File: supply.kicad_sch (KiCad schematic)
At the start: 35 parts

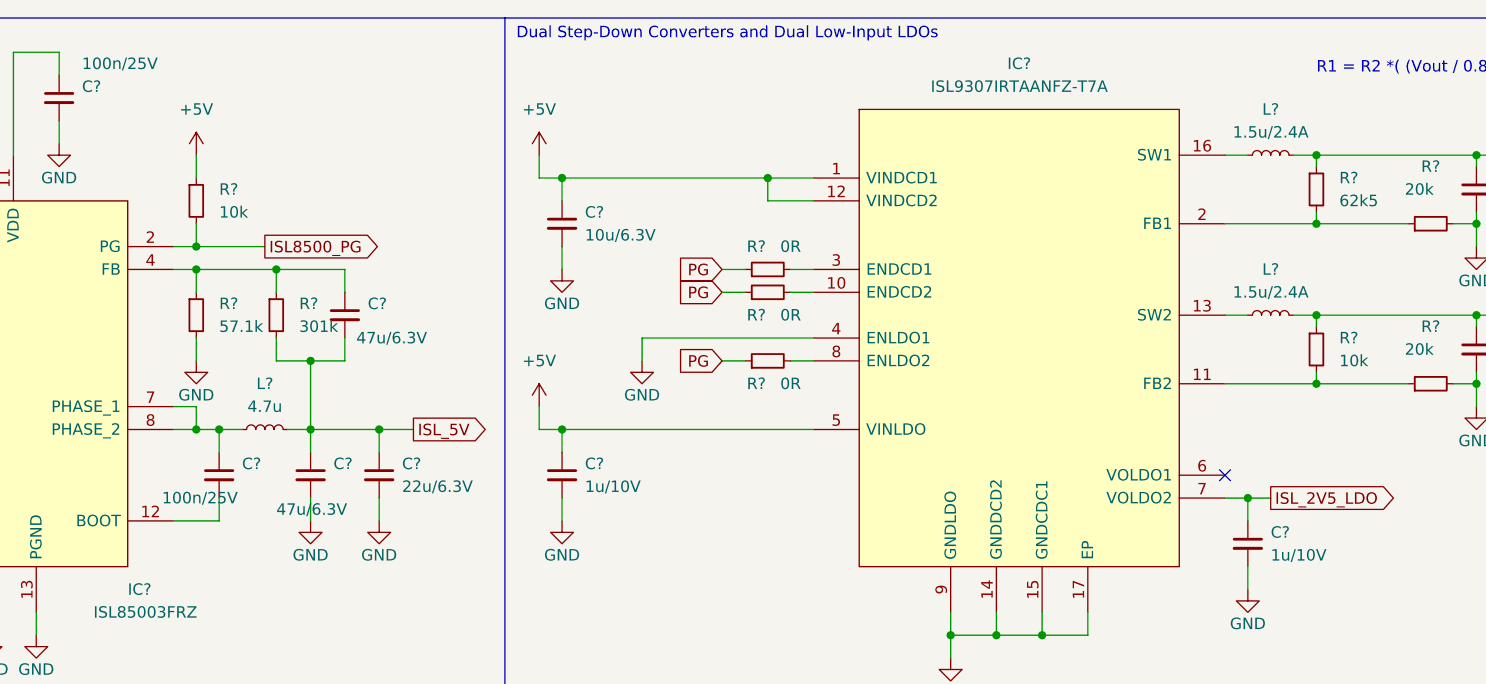
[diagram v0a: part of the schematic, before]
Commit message: added missing MNR && footprint to inductor added footprint to test points
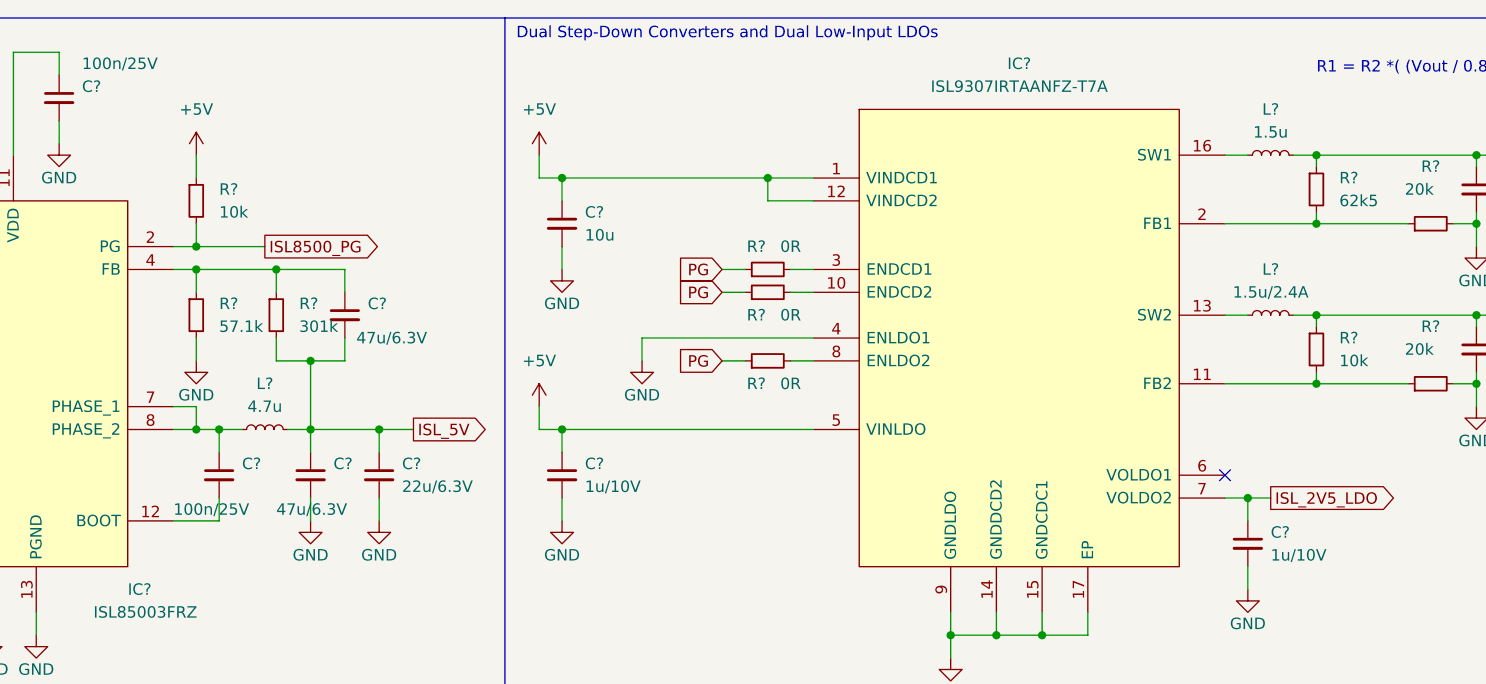
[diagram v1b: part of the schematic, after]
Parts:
- removed C?: 1u/10V, Capacitor_SMD:C_0603_1608Metric_Pad1.08x0.95mm_HandSolder, symbol Device:C_Small
- removed C?: 100n/25V, Capacitor_SMD:C_0603_1608Metric_Pad1.08x0.95mm_HandSolder, symbol Device:C_Small
- added C?: 100n/25V, Capacitor_SMD:C_0603_1608Metric_Pad1.08x0.95mm_HandSolder, symbol Device:C_Small
- added C?: 1u/10V, Capacitor_SMD:C_0603_1608Metric_Pad1.08x0.95mm_HandSolder, symbol Device:C_Small
- C?: value 10u/6.3V -> 10u
- L?: value 1.5u/2.4A -> 1.5u
- L?: footprint (none) -> supply:NR5040T4R7N; MNR (none) -> 963-NR5040T4R7N
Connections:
- net +5V: now also C?.1
- net GND: now also C?.2
- net at IC?.12 (BOOT): now also C?.2
- net at IC?.7 (PHASE_1), IC?.8 (PHASE_2), L?.1: now also C?.1
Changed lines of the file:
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@@
       (effects (font (size 1.27 1.27)) (justify left))
     )
-    (property "Value" "10u/6.3V" (id 1) (at 135.89 49.5362 0)
+    (property "Value" "10u" (id 1) (at 135.89 49.5362 0)
       (effects (font (size 1.27 1.27)) (justify left))
     )
@@
     (in_bom yes) (on_board yes) (fields_autoplaced)
     (property "Reference" "L?" (id 0) (at 212.09 35.56 90))
-    (property "Value" "1.5u/2.4A" (id 1) (at 212.09 38.1 90))
+    (property "Value" "1.5u" (id 1) (at 212.09 38.1 90))
     (property "Footprint" "Inductor_SMD:L_1008_2520Metric_Pad1.43x2.20mm_HandSolder" (id 2) (at 212.09 40.64 0)
       (effects (font (size 1.27 1.27)) hide)
@@
     )
     (property "MNR" " 963-MAKK2520H1R5M " (id 5) (at 212.09 40.64 90)
-      (effects (font (size 1.27 1.27)) hide)
-    )
-    (pin "1")
-    (pin "2")
-  )
-  (symbol (lib_id "Device:C_Small") (at 133.35 76.2 0) (unit 1)
-    (in_bom yes) (on_board yes) (fields_autoplaced)
-    (property "Reference" "C?" (id 0) (at 135.89 74.9362 0)
-      (effects (font (size 1.27 1.27)) (justify left))
-    )
-    (property "Value" "1u/10V" (id 1) (at 135.89 77.4762 0)
-      (effects (font (size 1.27 1.27)) (justify left))
-    )
-    (property "Footprint" "Capacitor_SMD:C_0603_1608Metric_Pad1.08x0.95mm_HandSolder" (id 2) (at 133.35 76.2 0)
-      (effects (font (size 1.27 1.27)) hide)
-    )
-    (property "Datasheet" "~" (id 3) (at 133.35 76.2 0)
-      (effects (font (size 1.27 1.27)) hide)
-    )
-    (property "MNR" " 187-CL10A105KP8NNWC " (id 5) (at 133.35 76.2 0)
       (effects (font (size 1.27 1.27)) hide)
     )
@@
     (pin "2")
   )
+  (symbol (lib_id "Device:C_Small") (at 95.25 76.2 0) (unit 1)
+    (in_bom yes) (on_board yes)
+    (property "Reference" "C?" (id 0) (at 97.79 74.9362 0)
+      (effects (font (size 1.27 1.27)) (justify left))
+    )
+    (property "Value" "100n/25V" (id 1) (at 90.17 80.01 0)
+      (effects (font (size 1.27 1.27)) (justify left))
+    )
+    (property "Footprint" "Capacitor_SMD:C_0603_1608Metric_Pad1.08x0.95mm_HandSolder" (id 2) (at 95.25 76.2 0)
+      (effects (font (size 1.27 1.27)) hide)
+    )
+    (property "Datasheet" "~" (id 3) (at 95.25 76.2 0)
+      (effects (font (size 1.27 1.27)) hide)
+    )
+    (property "MNR" " 603-CC603KRX7R8BB104 " (id 5) (at 95.25 76.2 0)
+      (effects (font (size 1.27 1.27)) hide)
+    )
+    (pin "1")
+    (pin "2")
+  )
   (symbol (lib_id "power:+5V") (at 114.3 114.3 0) (unit 1)
     (in_bom yes) (on_board yes) (fields_autoplaced)
@@
     (property "Reference" "L?" (id 0) (at 100.33 66.04 90))
     (property "Value" "4.7u" (id 1) (at 100.33 68.58 90))
-    (property "Footprint" "" (id 2) (at 100.33 71.12 0)
+    (property "Footprint" "supply:NR5040T4R7N" (id 2) (at 100.33 71.12 0)
       (effects (font (size 1.27 1.27)) hide)
     )
     (property "Datasheet" "~" (id 3) (at 100.33 71.12 0)
+      (effects (font (size 1.27 1.27)) hide)
+    )
+    (property "MNR" " 963-NR5040T4R7N " (id 5) (at 100.33 71.12 90)
       (effects (font (size 1.27 1.27)) hide)
     )
@@
     (pin "1")
   )
-  (symbol (lib_id "Device:C_Small") (at 95.25 76.2 0) (unit 1)
-    (in_bom yes) (on_board yes)
-    (property "Reference" "C?" (id 0) (at 97.79 74.9362 0)
-      (effects (font (size 1.27 1.27)) (justify left))
-    )
-    (property "Value" "100n/25V" (id 1) (at 88.9 78.74 0)
-      (effects (font (size 1.27 1.27)) (justify left))
-    )
-    (property "Footprint" "Capacitor_SMD:C_0603_1608Metric_Pad1.08x0.95mm_HandSolder" (id 2) (at 95.25 76.2 0)
-      (effects (font (size 1.27 1.27)) hide)
-    )
-    (property "Datasheet" "~" (id 3) (at 95.25 76.2 0)
-      (effects (font (size 1.27 1.27)) hide)
-    )
-    (property "MNR" " 603-CC603KRX7R8BB104 " (id 5) (at 95.25 76.2 0)
-      (effects (font (size 1.27 1.27)) hide)
-    )
-    (pin "1")
-    (pin "2")
-  )
   (symbol (lib_id "Device:R_Small") (at 229.87 66.04 90) (unit 1)
     (in_bom yes) (on_board yes)
@@
     (pin "1")
   )
+  (symbol (lib_id "Device:C_Small") (at 133.35 76.2 0) (unit 1)
+    (in_bom yes) (on_board yes) (fields_autoplaced)
+    (property "Reference" "C?" (id 0) (at 135.89 74.9362 0)
+      (effects (font (size 1.27 1.27)) (justify left))
+    )
+    (property "Value" "1u/10V" (id 1) (at 135.89 77.4762 0)
+      (effects (font (size 1.27 1.27)) (justify left))
+    )
+    (property "Footprint" "Capacitor_SMD:C_0603_1608Metric_Pad1.08x0.95mm_HandSolder" (id 2) (at 133.35 76.2 0)
+      (effects (font (size 1.27 1.27)) hide)
+    )
+    (property "Datasheet" "~" (id 3) (at 133.35 76.2 0)
+      (effects (font (size 1.27 1.27)) hide)
+    )
+    (property "MNR" " 187-CL10A105KP8NNWC " (id 5) (at 133.35 76.2 0)
+      (effects (font (size 1.27 1.27)) hide)
+    )
+    (pin "1")
+    (pin "2")
+  )
   (symbol (lib_id "Device:R_Small") (at 156.21 55.88 90) (unit 1)

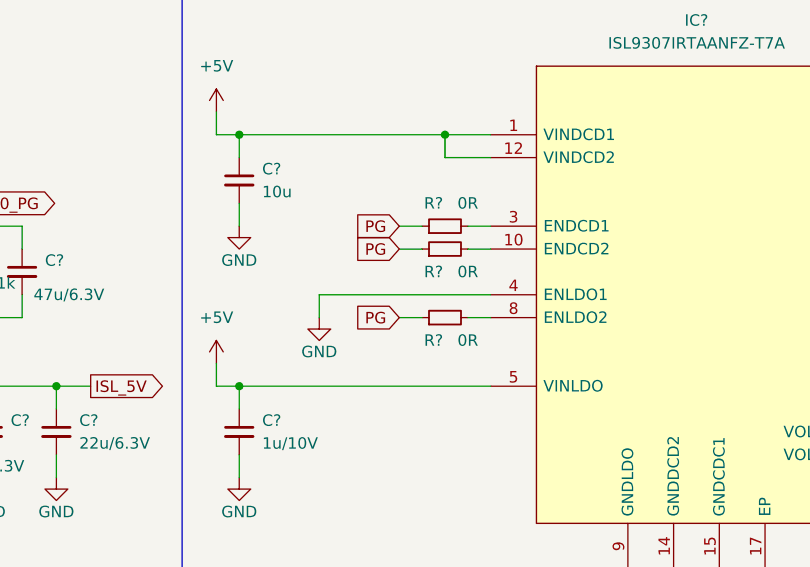
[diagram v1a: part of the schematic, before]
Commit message: fixed layout in fpga.kicad_sch
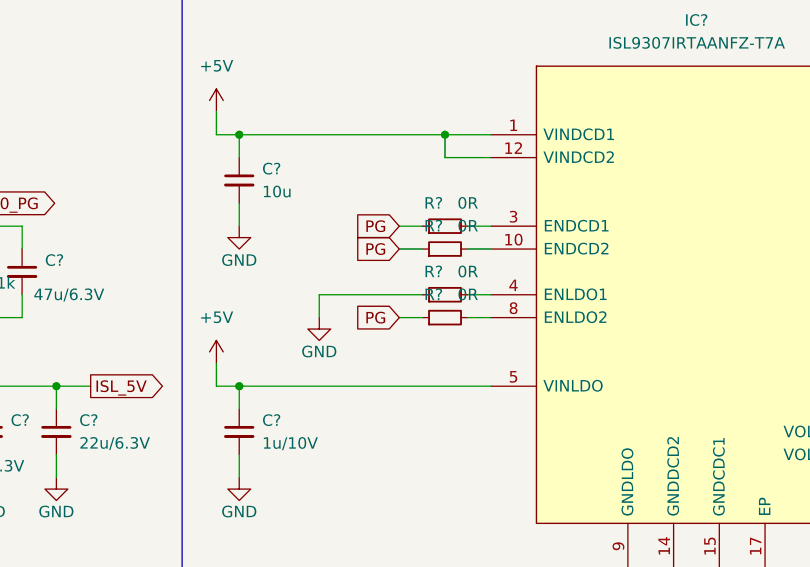
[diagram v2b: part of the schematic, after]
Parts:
- removed R?: 0R, Resistor_SMD:R_0603_1608Metric_Pad0.98x0.95mm_HandSolder, symbol Device:R_Small
- removed R?: 0R, aResistor_SMD:R_0603_1608Metric_Pad0.98x0.95mm_HandSolder, symbol Device:R_Small
- added R? (x3): 0R, Resistor_SMD:R_0603_1608Metric_Pad0.98x0.95mm_HandSolder, symbol Device:R_Small
- R?: MNR (none) -> 652-CR0603-J/-000ELF
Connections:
- net GND: now also R?.1; no longer IC?.4 (ENLDO1)
- net PG: now also R?.1, R?.1
- net at IC?.10 (ENDCD2): now also R?.2
- net at IC?.8 (ENLDO2): now also R?.2
- new net: IC?.4 (ENLDO1), R?.2
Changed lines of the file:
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@@
+    (stroke (width 0) (type default) (color 0 0 0 0))
+  )
+  (wire (pts (xy 158.75 60.96) (xy 161.29 60.96))
     (stroke (width 0) (type default) (color 0 0 0 0))
   )
@@
     (stroke (width 0) (type default) (color 0 0 0 0))
   )
+  (wire (pts (xy 142.24 60.96) (xy 153.67 60.96))
+    (stroke (width 0) (type default) (color 0 0 0 0))
+  )
   (polyline (pts (xy 139.7 101.6) (xy 140.97 101.6))
     (stroke (width 0) (type default) (color 0 0 0 0))
@@
   )
   (wire (pts (xy 50.8 138.43) (xy 53.34 138.43))
-    (stroke (width 0) (type default) (color 0 0 0 0))
-  )
-  (wire (pts (xy 142.24 60.96) (xy 161.29 60.96))
     (stroke (width 0) (type default) (color 0 0 0 0))
   )
@@
     )
     (pin "1")
+  )
+  (symbol (lib_id "Device:R_Small") (at 156.21 63.5 90) (unit 1)
+    (in_bom yes) (on_board yes)
+    (property "Reference" "R?" (id 0) (at 154.94 60.96 90))
+    (property "Value" "0R" (id 1) (at 158.75 60.96 90))
+    (property "Footprint" "Resistor_SMD:R_0603_1608Metric_Pad0.98x0.95mm_HandSolder" (id 2) (at 156.21 63.5 0)
+      (effects (font (size 1.27 1.27)) hide)
+    )
+    (property "Datasheet" "~" (id 3) (at 156.21 63.5 0)
+      (effects (font (size 1.27 1.27)) hide)
+    )
+    (property "MNR" " 652-CR0603-J/-000ELF " (id 5) (at 156.21 63.5 90)
+      (effects (font (size 1.27 1.27)) hide)
+    )
+    (pin "1")
+    (pin "2")
   )
   (symbol (lib_id "power:GND") (at 133.35 53.34 0) (unit 1)
@@
     (pin "2")
   )
-  (symbol (lib_id "Device:R_Small") (at 156.21 63.5 90) (unit 1)
-    (in_bom yes) (on_board yes)
-    (property "Reference" "R?" (id 0) (at 154.94 66.04 90))
-    (property "Value" "0R" (id 1) (at 158.75 66.04 90))
-    (property "Footprint" "Resistor_SMD:R_0603_1608Metric_Pad0.98x0.95mm_HandSolder" (id 2) (at 156.21 63.5 0)
-      (effects (font (size 1.27 1.27)) hide)
-    )
-    (property "Datasheet" "~" (id 3) (at 156.21 63.5 0)
-      (effects (font (size 1.27 1.27)) hide)
-    )
-    (pin "1")
-    (pin "2")
-  )
   (symbol (lib_id "Device:R_Small") (at 217.17 62.23 0) (unit 1)
     (in_bom yes) (on_board yes) (fields_autoplaced)
@@
     )
     (pin "1")
+  )
+  (symbol (lib_id "Device:R_Small") (at 156.21 55.88 90) (unit 1)
+    (in_bom yes) (on_board yes)
+    (property "Reference" "R?" (id 0) (at 154.94 53.34 90))
+    (property "Value" "0R" (id 1) (at 158.75 53.34 90))
+    (property "Footprint" "Resistor_SMD:R_0603_1608Metric_Pad0.98x0.95mm_HandSolder" (id 2) (at 156.21 55.88 0)
+      (effects (font (size 1.27 1.27)) hide)
+    )
+    (property "Datasheet" "~" (id 3) (at 156.21 55.88 0)
+      (effects (font (size 1.27 1.27)) hide)
+    )
+    (property "MNR" " 652-CR0603-J/-000ELF " (id 5) (at 156.21 55.88 90)
+      (effects (font (size 1.27 1.27)) hide)
+    )
+    (pin "1")
+    (pin "2")
   )
   (symbol (lib_id "power:+3V3") (at 50.8 127 0) (unit 1)
@@
       (effects (font (size 1.27 1.27)) hide)
     )
+    (property "MNR" " 652-CR0603-J/-000ELF " (id 5) (at 156.21 53.34 90)
+      (effects (font (size 1.27 1.27)) hide)
+    )
     (pin "1")
     (pin "2")
@@
     (pin "2")
   )
+  (symbol (lib_id "Device:R_Small") (at 156.21 60.96 90) (unit 1)
+    (in_bom yes) (on_board yes)
+    (property "Reference" "R?" (id 0) (at 154.94 58.42 90))
+    (property "Value" "0R" (id 1) (at 158.75 58.42 90))
+    (property "Footprint" "Resistor_SMD:R_0603_1608Metric_Pad0.98x0.95mm_HandSolder" (id 2) (at 156.21 60.96 0)
+      (effects (font (size 1.27 1.27)) hide)
+    )
+    (property "Datasheet" "~" (id 3) (at 156.21 60.96 0)
+      (effects (font (size 1.27 1.27)) hide)
+    )
+    (property "MNR" " 652-CR0603-J/-000ELF " (id 5) (at 156.21 60.96 90)
+      (effects (font (size 1.27 1.27)) hide)
+    )
+    (pin "1")
+    (pin "2")
+  )
   (symbol (lib_id "Device:C_Small") (at 95.25 76.2 0) (unit 1)
     (in_bom yes) (on_board yes)
@@
       (effects (font (size 1.27 1.27)) hide)
     )
-    (pin "1")
-    (pin "2")
-  )
-  (symbol (lib_id "Device:R_Small") (at 156.21 55.88 90) (unit 1)
-    (in_bom yes) (on_board yes)
-    (property "Reference" "R?" (id 0) (at 154.94 58.42 90))
-    (property "Value" "0R" (id 1) (at 158.75 58.42 90))
-    (property "Footprint" "aResistor_SMD:R_0603_1608Metric_Pad0.98x0.95mm_HandSolder" (id 2) (at 156.21 55.88 0)
-      (effects (font (size 1.27 1.27)) hide)
-    )
-    (property "Datasheet" "~" (id 3) (at 156.21 55.88 0)
-      (effects (font (size 1.27 1.27)) hide)
-    )

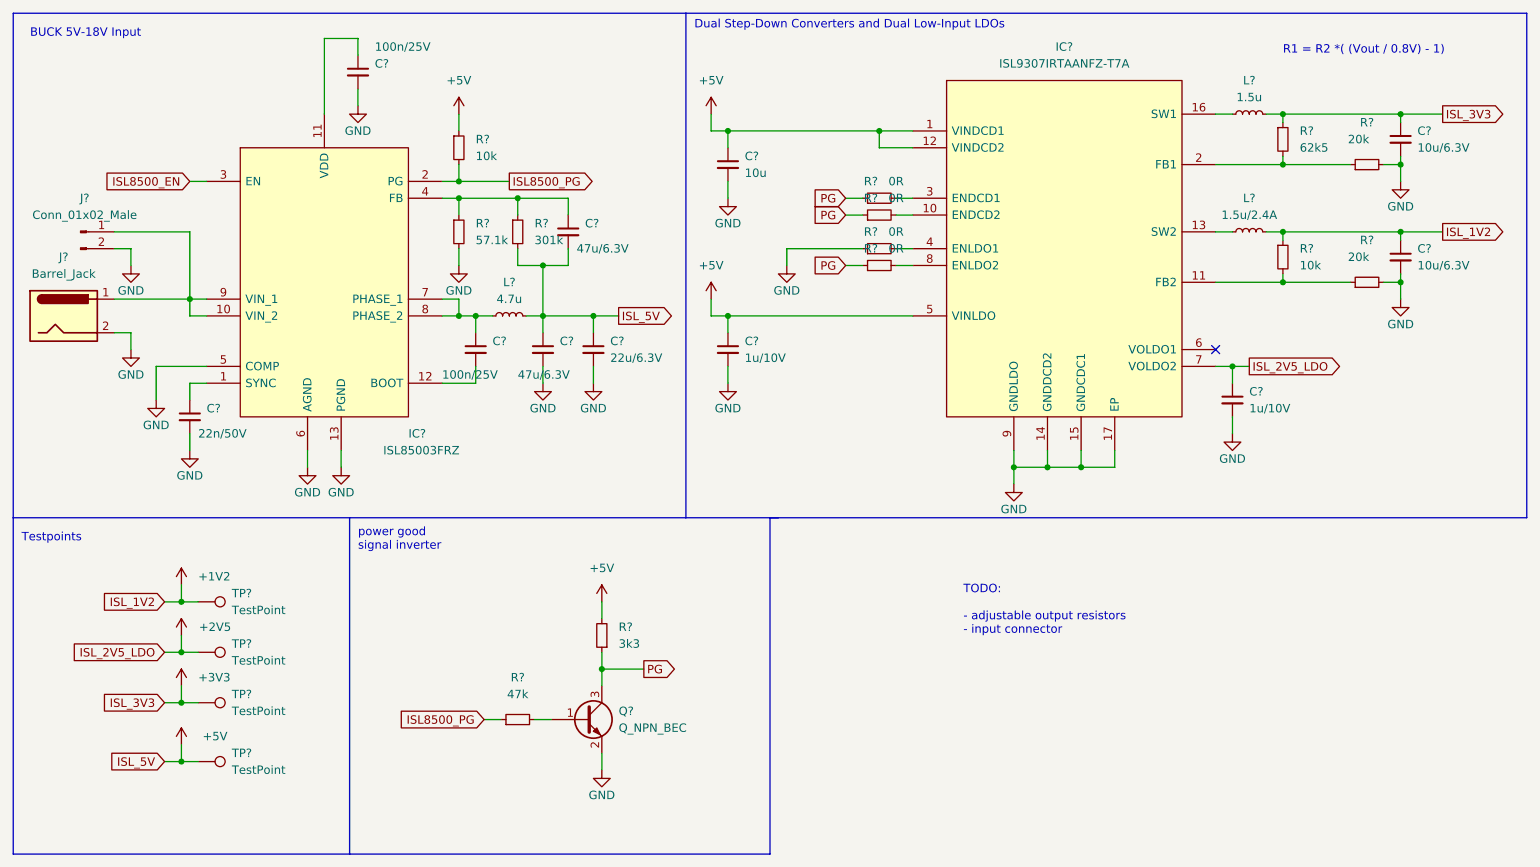
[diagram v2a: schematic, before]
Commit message: assigned some missing footprints
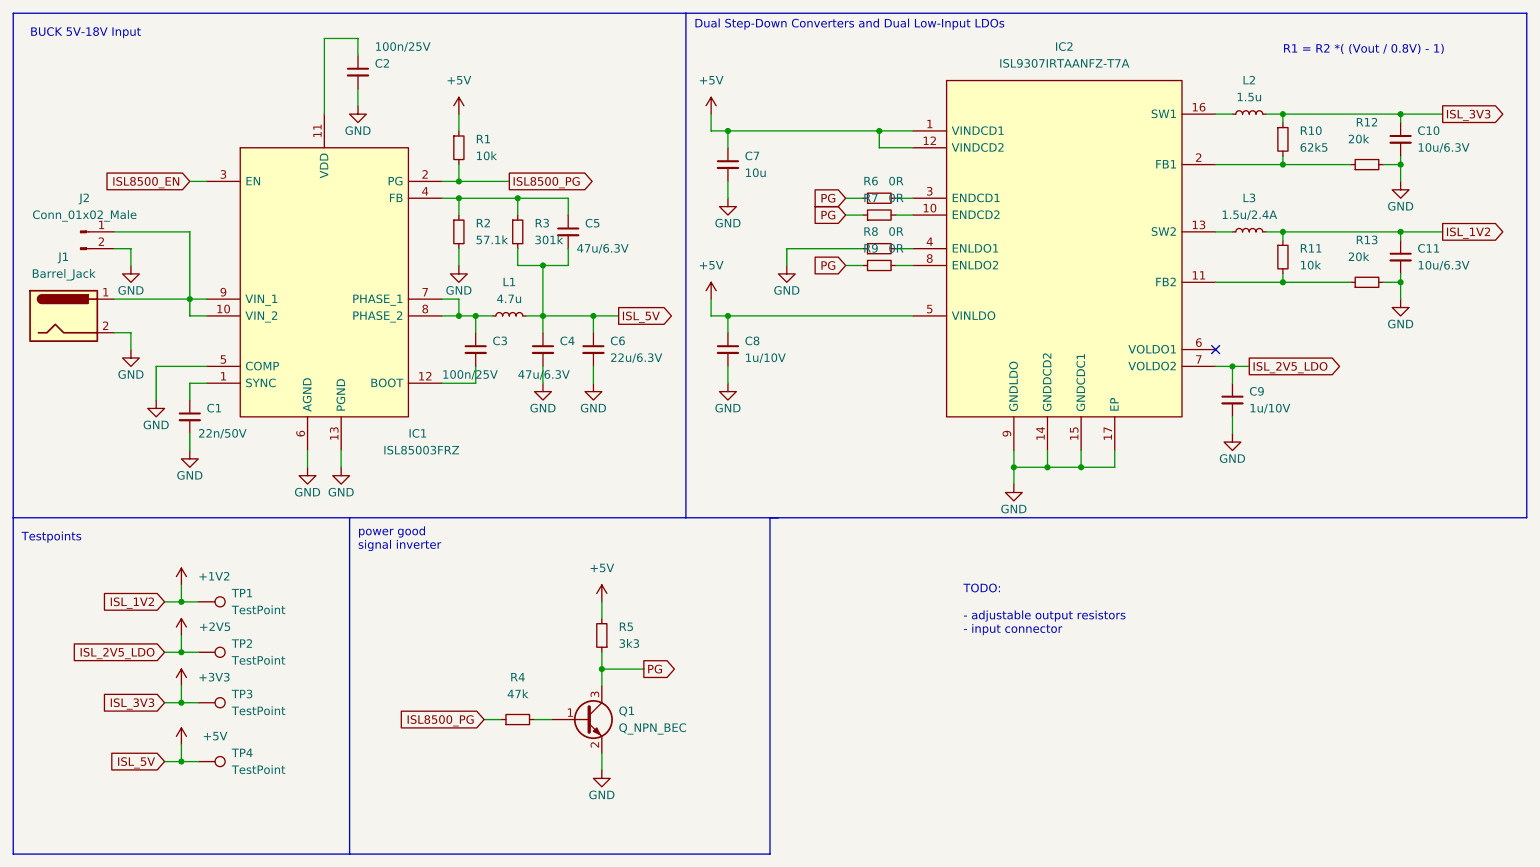
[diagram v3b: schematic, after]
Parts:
- IC1: renamed from IC?; footprint SON50P300X400X90-13N -> supply:SON50P300X400X90-13N
- J2: renamed from J?; footprint (none) -> Connector_PinHeader_2.54mm:PinHeader_1x02_P2.54mm_Vertical
- gave numbers to parts that had none: 34

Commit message: update footprints for fpga
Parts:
- J1: footprint (none) -> SamacSys_Parts:PJ063BH
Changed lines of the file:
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@@
     (property "Reference" "J1" (id 0) (at 33.02 62.23 0))
     (property "Value" "Barrel_Jack" (id 1) (at 33.02 64.77 0))
-    (property "Footprint" "" (id 2) (at 34.29 72.136 0)
+    (property "Footprint" "SamacSys_Parts:PJ063BH" (id 2) (at 34.29 72.136 0)
       (effects (font (size 1.27 1.27)) hide)
     )
